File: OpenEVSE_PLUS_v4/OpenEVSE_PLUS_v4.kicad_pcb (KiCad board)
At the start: 2 copper layers, 65.3 x 44.9 mm, 68 parts, among them IC1 MID400, IC2 ATMEGA328P-AU, IC3 LM358, IC4 LF353, IC5 AQH1213, Q1 16000, Q2 2222A, Q3 2222A

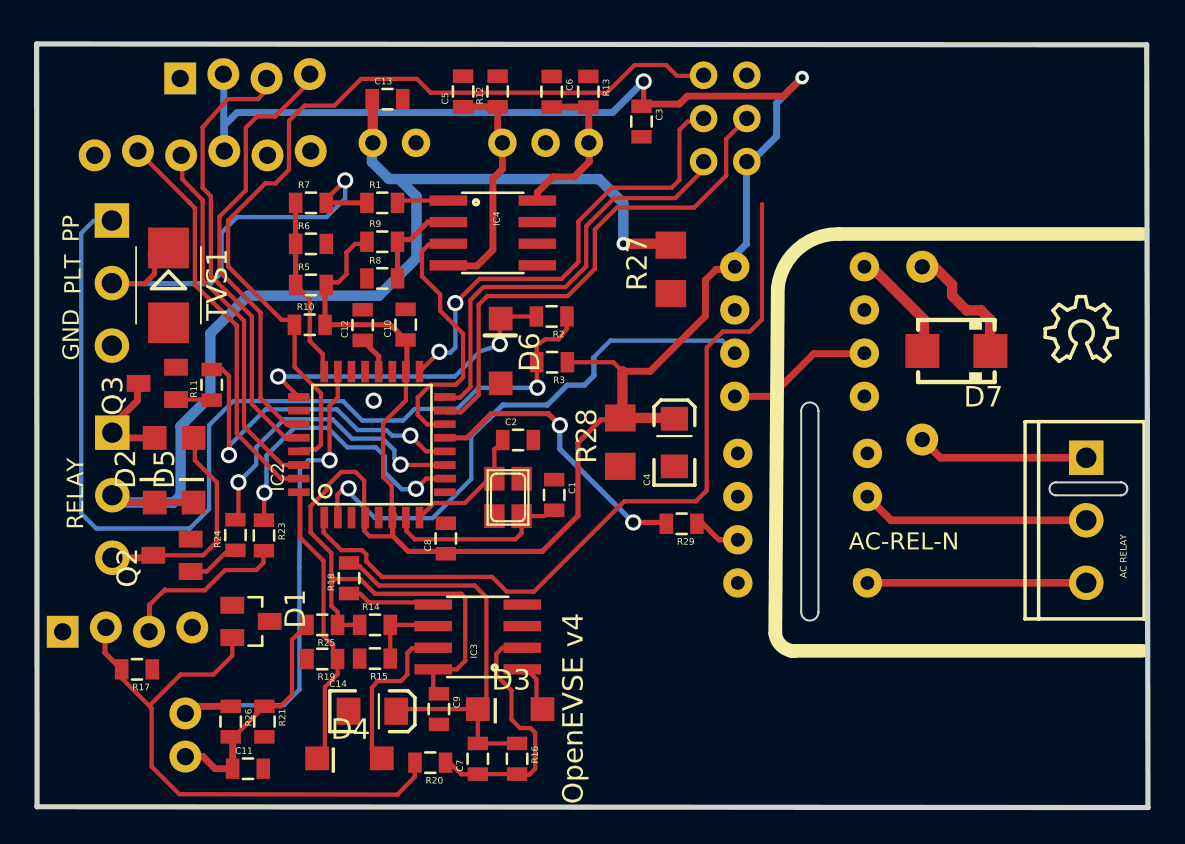
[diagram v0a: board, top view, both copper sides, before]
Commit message: updated footprints to kicad
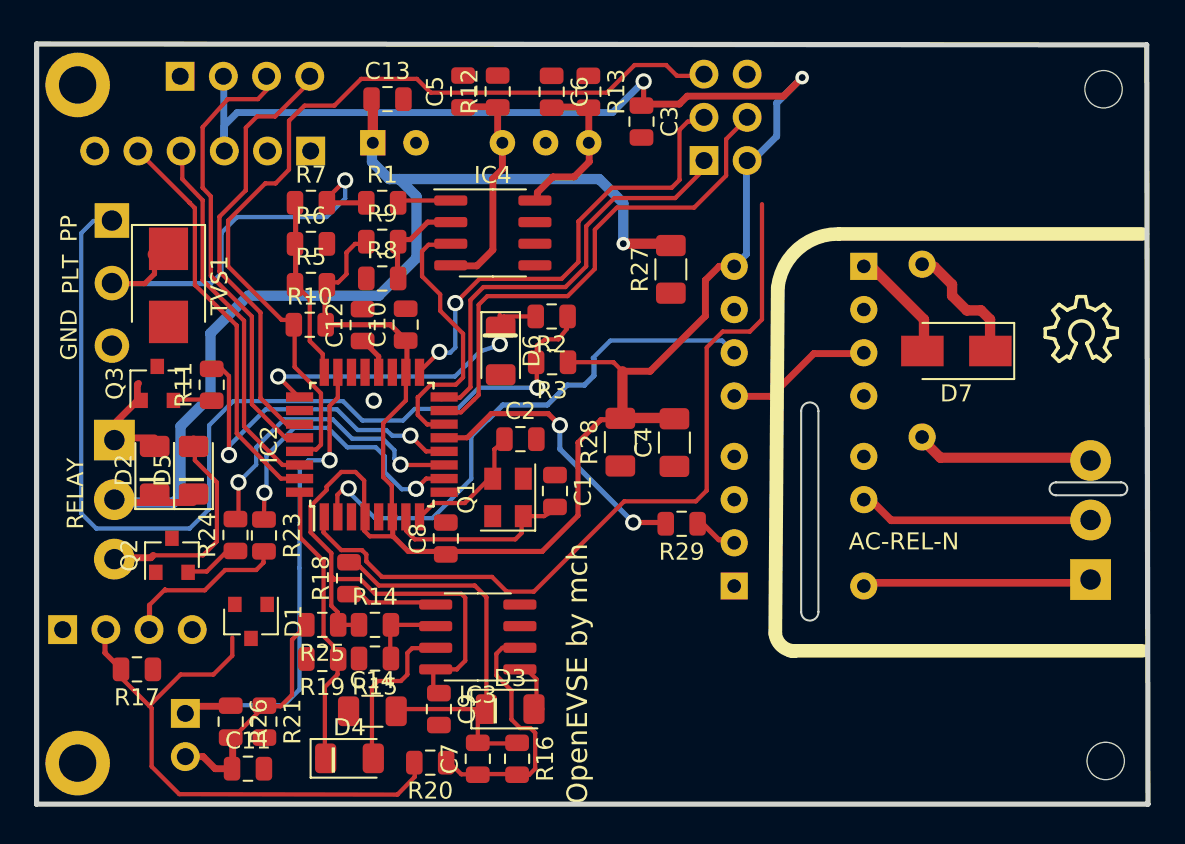
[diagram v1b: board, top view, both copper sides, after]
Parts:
- added H1: MountingHole_Pad, MountingHole:MountingHole_2.2mm_M2_DIN965_Pad, F.Cu at (118.2, 85.0)
- added H2: MountingHole_Pad, MountingHole:MountingHole_2.2mm_M2_DIN965_Pad, F.Cu at (118.2, 124.8)
- added H3: MountingHole, MountingHole:MountingHole_2.2mm_M2, F.Cu at (178.7, 124.7)
- added H4: MountingHole, MountingHole:MountingHole_2.2mm_M2, F.Cu at (178.6, 85.2)
- .1: footprint OpenEVSE_PLUS_v4:1X06_LOCK -> Connector_PinHeader_2.54mm:PinHeader_1x06_P2.54mm_Vertical
- A_CT1: footprint OpenEVSE_PLUS_v4:1X02 -> Connector_PinHeader_2.54mm:PinHeader_1x02_P2.54mm_Vertical
- C1, C10, C11, C12, C13, C2, C3, C5, C6, C7, C8, C9: footprint OpenEVSE_PLUS_v4:0805 -> Capacitor_SMD:C_0805_2012Metric
- C14, C4: footprint OpenEVSE_PLUS_v4:EIA3216 -> Capacitor_SMD:C_1206_3216Metric
- D1, Q2, Q3: footprint OpenEVSE_PLUS_v4:SOT23 -> Package_TO_SOT_SMD:SOT-23
- D2, D3, D4, D5, D6: footprint OpenEVSE_PLUS_v4:SOD123 -> Diode_SMD:D_1206_3216Metric
- D7: footprint OpenEVSE_PLUS_v4:SMA -> Diode_SMD:D_SMA
- DCDC1: value MD112D-12E -> AIMTEC; footprint OpenEVSE_PLUS_v4:DCDC_SIP -> Converter_DCDC:Converter_DCDC_muRata_NMAxxxxSC_THT
- G_CT1, I2C1: footprint OpenEVSE_PLUS_v4:1X04_LOCK -> Connector_PinHeader_2.54mm:PinHeader_1x04_P2.54mm_Vertical
- IC1: footprint OpenEVSE_PLUS_v4:DIP08 -> Package_DIP:DIP-8_W7.62mm
- IC2: footprint OpenEVSE_PLUS_v4:TQFP32-08 -> Package_QFP:TQFP-32_7x7mm_P0.8mm
- IC3, IC4: footprint OpenEVSE_PLUS_v4:SO08 -> Package_SO:SOIC-8_3.9x4.9mm_P1.27mm
- IC5: footprint OpenEVSE_PLUS_v4:DIP7 -> Package_DIP:DIP-8-N7_W7.62mm
- ISP1: footprint OpenEVSE_PLUS_v4:AVRISP -> Connector_PinHeader_2.54mm:PinHeader_2x03_P2.54mm_Vertical
- Q1: footprint OpenEVSE_PLUS_v4:NX3225 -> Crystal:Crystal_SMD_EuroQuartz_MT-4Pin_3.2x2.5mm
- R1, R10, R11, R12, R13, R14, R15, R16, R17, R18, R19, R2, R20, R21, R23, R24, R25, R26, R29, R3, R5, R6, R7, R8, R9: footprint OpenEVSE_PLUS_v4:0805 -> Resistor_SMD:R_0805_2012Metric
- R27, R28: footprint OpenEVSE_PLUS_v4:R1206 -> Resistor_SMD:R_1206_3216Metric
- R4: value 47K -> 56k 1W; footprint OpenEVSE_PLUS_v4:AXIAL-0.4 -> Resistor_THT:R_Axial_DIN0207_L6.3mm_D2.5mm_P10.16mm_Horizontal
- RELAY1: footprint OpenEVSE_PLUS_v4:SCREWTERMINAL-3.5MM-3_LOCK.007S -> TerminalBlock_Phoenix:TerminalBlock_Phoenix_PT-1,5-3-3.5-H_1x03_P3.50mm_Horizontal
- RELAY2: renamed from AC RELAY; footprint OpenEVSE_PLUS_v4:SCREWTERMINAL-3.5MM-3_LOCK.007S -> TerminalBlock_Phoenix:TerminalBlock_Phoenix_PT-1,5-3-3.5-H_1x03_P3.50mm_Horizontal; moved to B.Cu
- TVS1: footprint OpenEVSE_PLUS_v4:SMB -> Diode_SMD:D_SMB
- moved RELAY2 6.99 mm to (177.8, 114.0), turned to 90 degrees
- moved IC5 5.66 mm to (156.8, 114.4), turned to 0 degrees
- moved IC1 5.38 mm to (164.5, 95.6), turned to 180 degrees
- moved R4 4.93 mm to (167.9, 105.7)
- moved ISP1 2.77 mm to (155.1, 89.4)
- moved RELAY1 0.29 mm to (120.4, 105.8)
- moved C1 0.24 mm to (146.3, 108.8)
- moved C2 0.15 mm to (144.3, 105.8)
- turned .1 to 90 degrees
- turned A_CT1 to 180 degrees
- turned DCDC1 to 270 degrees
- turned G_CT1 to 270 degrees
- turned I2C1 to 270 degrees
- turned IC3 to 180 degrees
- turned IC4 to 0 degrees
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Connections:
- RELAY2 pad 1: /ACTST -> /AC-N2
- RELAY2 pad 3: /AC-N2 -> /ACTST
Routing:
- net (no net): track 0.00 -> 41.1 mm
- net Net-(D5-PadA): track 13.5 -> 0.00 mm
- net /ACTST: track 10.1 -> 0.00 mm
- net Net-(D4-PadA): track 9.75 -> 0.00 mm
- net Net-(D7-PadA): track 6.68 -> 0.00 mm
- net Net-(D3-PadA): track 2.98 -> 0.00 mm
- net Net-(D7-PadC): track 7.65 -> 10.1 mm
- net GND: track 9.23 -> 8.67 mm
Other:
- board size 65.3 x 44.9 mm -> 65.4 x 44.7 mm
- board text added: "OpenEVSE by mch"
- board text removed: "AC_TEST"
- board text removed: "H"
- board text removed: "N"
- board text removed: "OpenEVSE v4"

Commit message: added 3.3 and 5v regulators
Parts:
- added C15: 100uF, Capacitor_THT:CP_Radial_D5.0mm_P2.50mm, B.Cu at (171.8, 125.0)
- added C16: 22uF, Capacitor_SMD:C_1206_3216Metric, F.Cu at (177.4, 90.0)
- added J1: Conn_02x04_Odd_Even, Connector_PinSocket_2.54mm:PinSocket_2x04_P2.54mm_Vertical, B.Cu at (154.6, 125.5)
- added R22: 10k, Resistor_SMD:R_0805_2012Metric, F.Cu at (159.4, 124.0)
- added U1: SPX3819M5-L-3-3, Package_TO_SOT_SMD:SOT-23-5, F.Cu at (164.3, 122.9)
- added U2: AMS1117-5.0, Package_TO_SOT_SMD:SOT-223-3_TabPin2, F.Cu at (170.0, 87.5)
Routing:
- net +5V: track 155.8 -> 181.2 mm, vias 2 -> 3
- net GND: track 8.67 -> 33.5 mm, vias 1 -> 17
- net /3-3v: track 0.00 -> 22.9 mm
- net /CH_PD: track 0.00 -> 8.18 mm
- net /BTN1: track 46.7 -> 39.9 mm
- net Net-(D2-PadA): track 6.15 -> 5.11 mm
- added copper zone on B.Cu, net GND
- added copper zone on F.Cu, net GND
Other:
- board text added: "OpenEVSE"
- board text added: "OpenEVSE by martii"
- board text removed: "OpenEVSE by mch"
